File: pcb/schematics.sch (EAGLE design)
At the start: 8 parts, among them IC1 MEGA8-P

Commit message: Update pcb
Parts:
- removed MICROUSB: 1X5, adafruit:1X5
- removed RTC: 1X4-3.5MM, adafruit:1X4-3.5MM
- removed S1: (no value), switch-omron:40-XX
- added BTN: (no value), switch-omron:10-XX
- added X1, X2: 22-23-2051, con-molex:22-23-2051
- SOIL: value 1X4-3.5MM -> 1X4-BIG; device adafruit:1X4-3.5MM -> adafruit:1X4-BIG
- renumbered R1 to BTNR
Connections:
- new net N$9: IC1.PC0(ADC0), SOIL.4
- net N$1: now also X1-4.S; no longer RTC.3
- net N$2: now also X1-3.S; no longer RTC.2
- net N$3: now also IC1.GND, X1-1.S, X2-1.S; no longer MICROUSB.1, RTC.1
- net N$5: now also BTN.S1, IC1.AVCC, X1-5.S, X2-5.S; no longer MICROUSB.5, RTC.4, S1.S1, SOIL.1
- net N$6: now also SOIL.1; no longer SOIL.4
- net N$7: now also BTN.S; no longer S1.S
- net N$8: now also BTN.P; no longer S1.P
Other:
- moved on the sheet: SOIL

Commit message: Update eagle files
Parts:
- added C1: (no value), rcl:C-EU025-025X050
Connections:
- removed net N$3: BTNR.2, IC1.GND, IC1.GND@1, SOIL.2, U$1.GND, U$2.GND, X1-1.S, X2-1.S
- new net GND: BTNR.2, C1.2, IC1.GND, IC1.GND@1, SOIL.2, U$1.GND, U$2.GND, X1-1.S, X2-1.S
- net N$5: now also C1.1
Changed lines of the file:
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@@
 <part name="X1" library="con-molex" library_urn="urn:adsk.eagle:library:165" deviceset="22-23-2051" device="" package3d_urn="urn:adsk.eagle:package:8078636/1"/>
 <part name="X2" library="con-molex" library_urn="urn:adsk.eagle:library:165" deviceset="22-23-2051" device="" package3d_urn="urn:adsk.eagle:package:8078636/1"/>
+<part name="C1" library="rcl" library_urn="urn:adsk.eagle:library:334" deviceset="C-EU" device="025-025X050" package3d_urn="urn:adsk.eagle:package:23629/2"/>
 </parts>
 <sheets>
@@
 <instance part="X2" gate="-5" x="-101.6" y="83.82" smashed="yes" rot="R180">
 <attribute name="NAME" x="-104.14" y="84.582" size="1.524" layer="95" rot="R180"/>
+</instance>
+<instance part="C1" gate="G$1" x="-91.44" y="78.74" smashed="yes">
+<attribute name="NAME" x="-89.916" y="79.121" size="1.778" layer="95"/>
+<attribute name="VALUE" x="-89.916" y="74.041" size="1.778" layer="96"/>
 </instance>
 </instances>
@@
 </segment>
 </net>
-<net name="N$3" class="0">
+<net name="GND" class="0">
 <segment>
 <pinref part="U$2" gate="G$1" pin="GND"/>
@@
 <wire x1="38.1" y1="33.02" x2="25.4" y2="33.02" width="0.1524" layer="91"/>
 <wire x1="25.4" y1="33.02" x2="25.4" y2="48.26" width="0.1524" layer="91"/>
-<wire x1="-99.06" y1="73.66" x2="-71.12" y2="73.66" width="0.1524" layer="91"/>
+<wire x1="-99.06" y1="73.66" x2="-91.44" y2="73.66" width="0.1524" layer="91"/>
 <junction x="-71.12" y="73.66"/>
 <pinref part="IC1" gate="G$1" pin="GND"/>
+<wire x1="-91.44" y1="73.66" x2="-71.12" y2="73.66" width="0.1524" layer="91"/>
 <wire x1="-71.12" y1="83.82" x2="-71.12" y2="109.22" width="0.1524" layer="91"/>
 <wire x1="-71.12" y1="109.22" x2="-63.5" y2="109.22" width="0.1524" layer="91"/>
@@
 <wire x1="38.1" y1="35.56" x2="43.18" y2="35.56" width="0.1524" layer="91"/>
 <pinref part="X2" gate="-1" pin="S"/>
+<pinref part="C1" gate="G$1" pin="2"/>
+<junction x="-91.44" y="73.66"/>
+<label x="-99.06" y="73.66" size="1.778" layer="95"/>
 </segment>
 </net>
@@
 <pinref part="X1" gate="-5" pin="S"/>
 <pinref part="X2" gate="-5" pin="S"/>
-<wire x1="-83.82" y1="83.82" x2="-99.06" y2="83.82" width="0.1524" layer="91"/>
+<wire x1="-83.82" y1="83.82" x2="-91.44" y2="83.82" width="0.1524" layer="91"/>
+<pinref part="C1" gate="G$1" pin="1"/>
+<wire x1="-91.44" y1="83.82" x2="-99.06" y2="83.82" width="0.1524" layer="91"/>
+<wire x1="-91.44" y1="81.28" x2="-91.44" y2="83.82" width="0.1524" layer="91"/>
+<junction x="-91.44" y="83.82"/>
 </segment>
 </net>
@@
 packages will not be understood (or retained) with this version.
 </note>
+<note version="8.4" severity="warning">
+Since Version 8.4, EAGLE supports properties for SPICE simulation.
+Probes in schematics and SPICE mapping objects found in parts and library devices
+will not be understood with this version. Update EAGLE to the latest version
+for full support of SPICE simulation.
+</note>
 </compatibility>

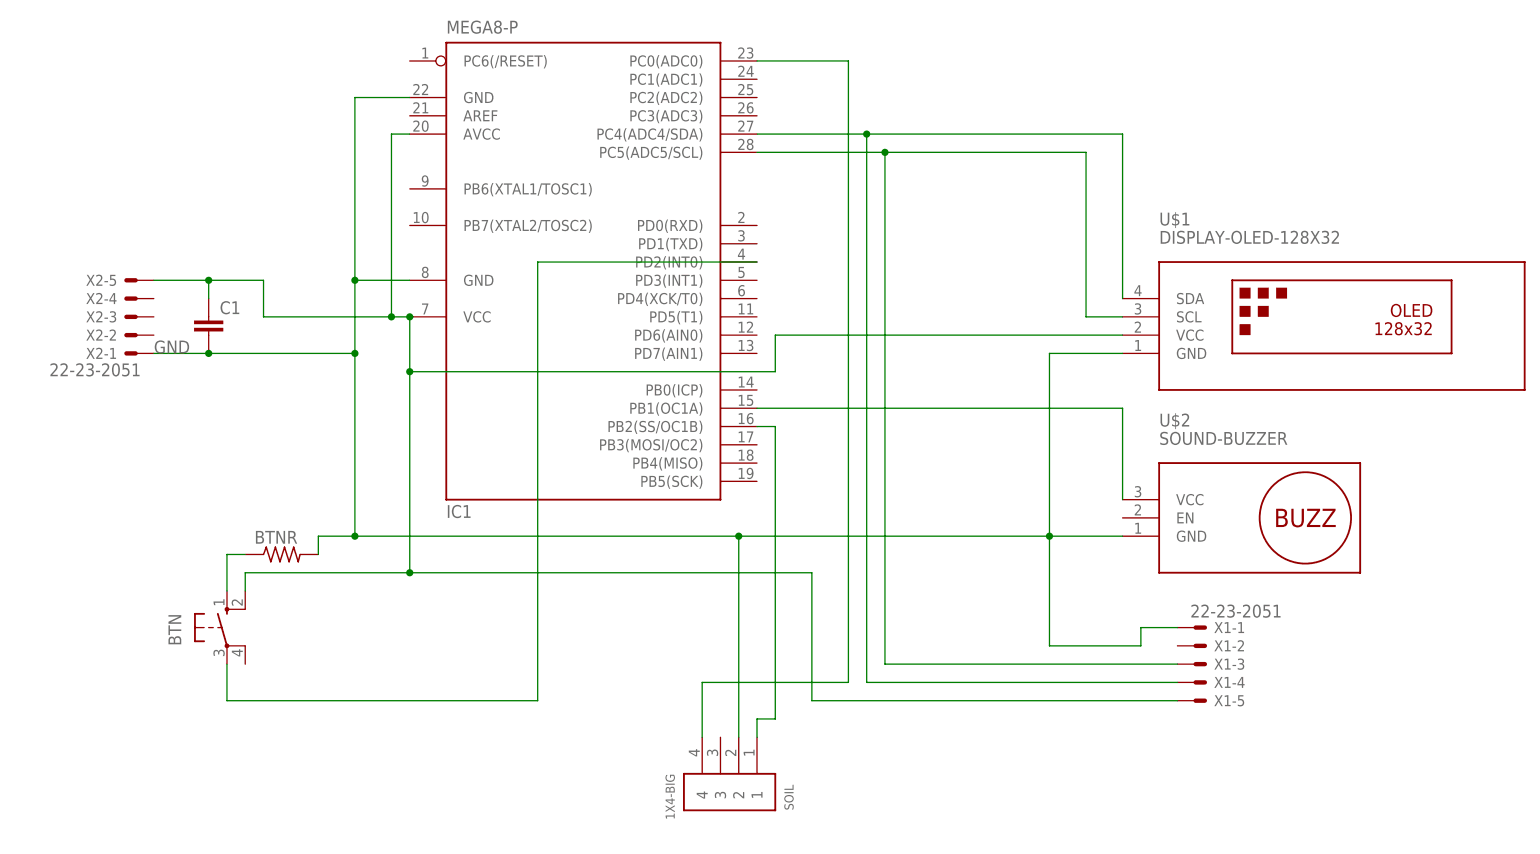
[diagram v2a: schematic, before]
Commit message: Add slide switch
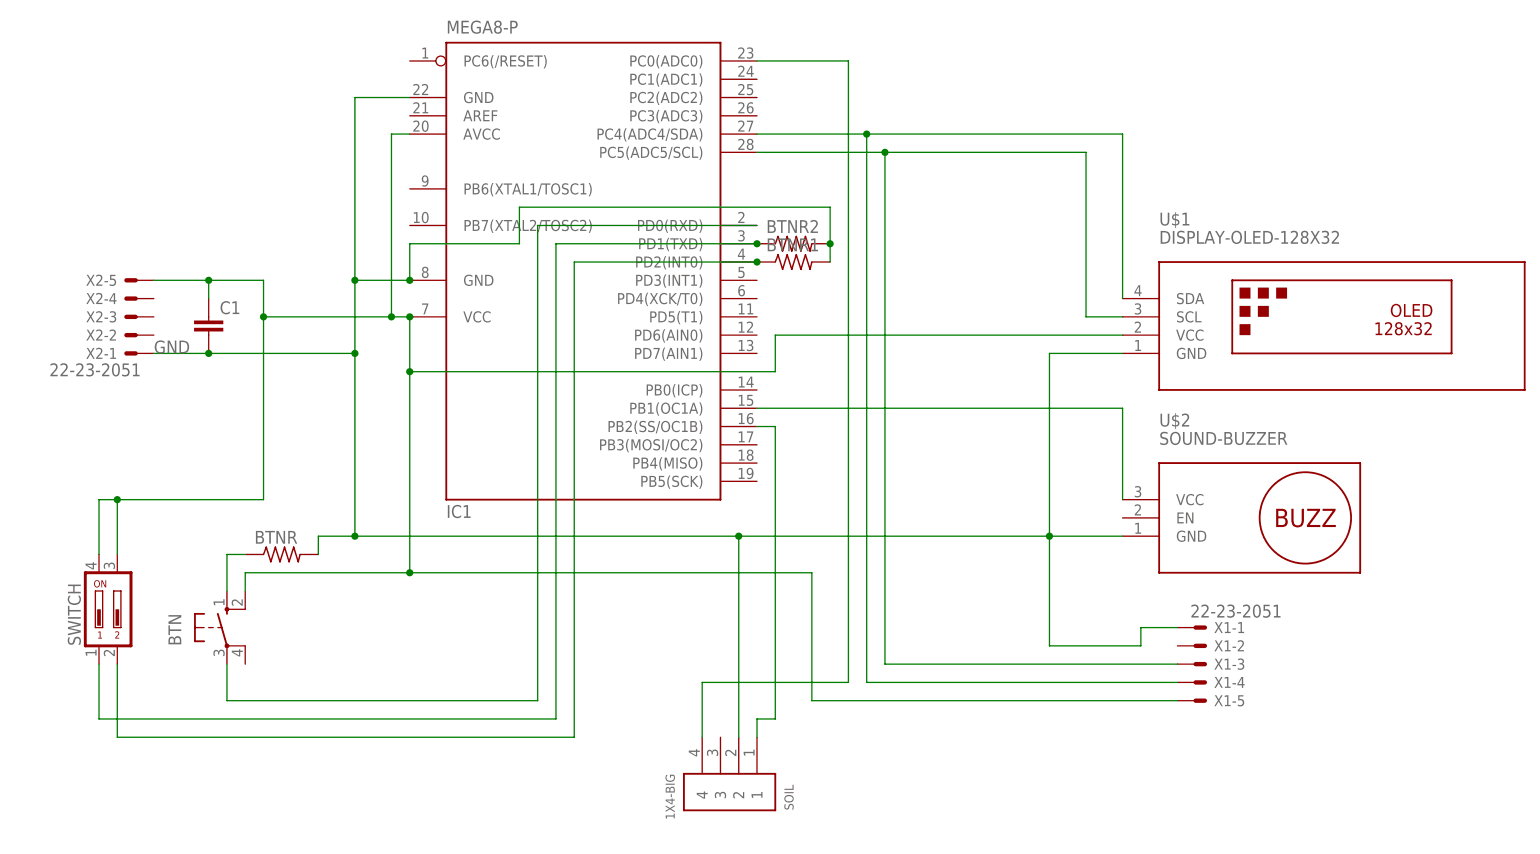
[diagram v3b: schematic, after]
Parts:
- added BTNR1, BTNR2: (no value), adafruit:R-US_0204/7
- added SWITCH: (no value), switch-dil:DIP02YL
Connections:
- new net N$10: BTNR1.1, IC1.PD2(INT0), SWITCH.2
- new net N$3: BTNR2.1, IC1.PD1(TXD), SWITCH.1
- net GND: now also BTNR1.2, BTNR2.2
- net N$5: now also SWITCH.3, SWITCH.4
- net N$8: now also IC1.PD0(RXD); no longer IC1.PD2(INT0)
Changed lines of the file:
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@@
 <part name="X2" library="con-molex" library_urn="urn:adsk.eagle:library:165" deviceset="22-23-2051" device="" package3d_urn="urn:adsk.eagle:package:8078636/1"/>
 <part name="C1" library="rcl" library_urn="urn:adsk.eagle:library:334" deviceset="C-EU" device="025-025X050" package3d_urn="urn:adsk.eagle:package:23629/2"/>
+<part name="SWITCH" library="switch-dil" library_urn="urn:adsk.eagle:library:375" deviceset="DIP02YL" device="" package3d_urn="urn:adsk.eagle:package:27254/2"/>
+<part name="BTNR1" library="adafruit" library_urn="urn:adsk.eagle:library:420" deviceset="R-US_" device="0204/7" package3d_urn="urn:adsk.eagle:package:6240596/1"/>
+<part name="BTNR2" library="adafruit" library_urn="urn:adsk.eagle:library:420" deviceset="R-US_" device="0204/7" package3d_urn="urn:adsk.eagle:package:6240596/1"/>
 </parts>
 <sheets>
@@
 <attribute name="NAME" x="-89.916" y="79.121" size="1.778" layer="95"/>
 <attribute name="VALUE" x="-89.916" y="74.041" size="1.778" layer="96"/>
+</instance>
+<instance part="SWITCH" gate="1" x="-106.68" y="38.1" smashed="yes">
+<attribute name="NAME" x="-109.22" y="33.02" size="1.778" layer="95" rot="R90"/>
+<attribute name="VALUE" x="-99.695" y="33.02" size="1.778" layer="96" rot="R90"/>
+</instance>
+<instance part="BTNR1" gate="G$1" x="-10.16" y="86.36" smashed="yes">
+<attribute name="NAME" x="-13.97" y="87.8586" size="1.778" layer="95"/>
+<attribute name="VALUE" x="-13.97" y="83.058" size="1.778" layer="96"/>
+</instance>
+<instance part="BTNR2" gate="G$1" x="-10.16" y="88.9" smashed="yes">
+<attribute name="NAME" x="-13.97" y="90.3986" size="1.778" layer="95"/>
+<attribute name="VALUE" x="-13.97" y="85.598" size="1.778" layer="96"/>
 </instance>
 </instances>
@@
 <junction x="-91.44" y="73.66"/>
 <label x="-99.06" y="73.66" size="1.778" layer="95"/>
+<wire x1="-63.5" y1="83.82" x2="-63.5" y2="88.9" width="0.1524" layer="91"/>
+<wire x1="-63.5" y1="88.9" x2="-48.26" y2="88.9" width="0.1524" layer="91"/>
+<junction x="-63.5" y="83.82"/>
+<wire x1="-48.26" y1="88.9" x2="-48.26" y2="93.98" width="0.1524" layer="91"/>
+<wire x1="-48.26" y1="93.98" x2="-5.08" y2="93.98" width="0.1524" layer="91"/>
+<pinref part="BTNR2" gate="G$1" pin="2"/>
+<wire x1="-5.08" y1="93.98" x2="-5.08" y2="88.9" width="0.1524" layer="91"/>
+<pinref part="BTNR1" gate="G$1" pin="2"/>
+<wire x1="-5.08" y1="86.36" x2="-5.08" y2="88.9" width="0.1524" layer="91"/>
+<junction x="-5.08" y="88.9"/>
 </segment>
 </net>
@@
 <wire x1="-91.44" y1="81.28" x2="-91.44" y2="83.82" width="0.1524" layer="91"/>
 <junction x="-91.44" y="83.82"/>
+<wire x1="-83.82" y1="78.74" x2="-83.82" y2="53.34" width="0.1524" layer="91"/>
+<junction x="-83.82" y="78.74"/>
+<pinref part="SWITCH" gate="1" pin="4"/>
+<wire x1="-83.82" y1="53.34" x2="-104.14" y2="53.34" width="0.1524" layer="91"/>
+<wire x1="-104.14" y1="53.34" x2="-106.68" y2="53.34" width="0.1524" layer="91"/>
+<wire x1="-106.68" y1="53.34" x2="-106.68" y2="45.72" width="0.1524" layer="91"/>
+<pinref part="SWITCH" gate="1" pin="3"/>
+<wire x1="-104.14" y1="45.72" x2="-104.14" y2="53.34" width="0.1524" layer="91"/>
+<junction x="-104.14" y="53.34"/>
 </segment>
 </net>
@@
 <net name="N$8" class="0">
 <segment>
-<pinref part="IC1" gate="G$1" pin="PD2(INT0)"/>
-<wire x1="-15.24" y1="86.36" x2="-45.72" y2="86.36" width="0.1524" layer="91"/>
-<wire x1="-45.72" y1="86.36" x2="-45.72" y2="25.4" width="0.1524" layer="91"/>
+<wire x1="-45.72" y1="91.44" x2="-45.72" y2="25.4" width="0.1524" layer="91"/>
 <wire x1="-45.72" y1="25.4" x2="-88.9" y2="25.4" width="0.1524" layer="91"/>
 <pinref part="BTN" gate="1" pin="P"/>
 <wire x1="-88.9" y1="25.4" x2="-88.9" y2="30.48" width="0.1524" layer="91"/>
+<pinref part="IC1" gate="G$1" pin="PD0(RXD)"/>
+<wire x1="-45.72" y1="91.44" x2="-15.24" y2="91.44" width="0.1524" layer="91"/>
 </segment>
 </net>
@@
 </segment>
 </net>
+<net name="N$3" class="0">
+<segment>
+<pinref part="IC1" gate="G$1" pin="PD1(TXD)"/>
+<wire x1="-15.24" y1="88.9" x2="-43.18" y2="88.9" width="0.1524" layer="91"/>
+<wire x1="-43.18" y1="88.9" x2="-43.18" y2="22.86" width="0.1524" layer="91"/>
+<pinref part="SWITCH" gate="1" pin="1"/>
+<wire x1="-43.18" y1="22.86" x2="-106.68" y2="22.86" width="0.1524" layer="91"/>
+<wire x1="-106.68" y1="22.86" x2="-106.68" y2="30.48" width="0.1524" layer="91"/>
+<pinref part="BTNR2" gate="G$1" pin="1"/>
+<junction x="-15.24" y="88.9"/>
+</segment>
+</net>
+<net name="N$10" class="0">
+<segment>
+<pinref part="SWITCH" gate="1" pin="2"/>
+<wire x1="-104.14" y1="30.48" x2="-104.14" y2="20.32" width="0.1524" layer="91"/>
+<wire x1="-104.14" y1="20.32" x2="-40.64" y2="20.32" width="0.1524" layer="91"/>
+<pinref part="IC1" gate="G$1" pin="PD2(INT0)"/>
+<wire x1="-40.64" y1="20.32" x2="-40.64" y2="86.36" width="0.1524" layer="91"/>
+<wire x1="-40.64" y1="86.36" x2="-15.24" y2="86.36" width="0.1524" layer="91"/>
+<pinref part="BTNR1" gate="G$1" pin="1"/>
+<junction x="-15.24" y="86.36"/>
+</segment>
+</net>

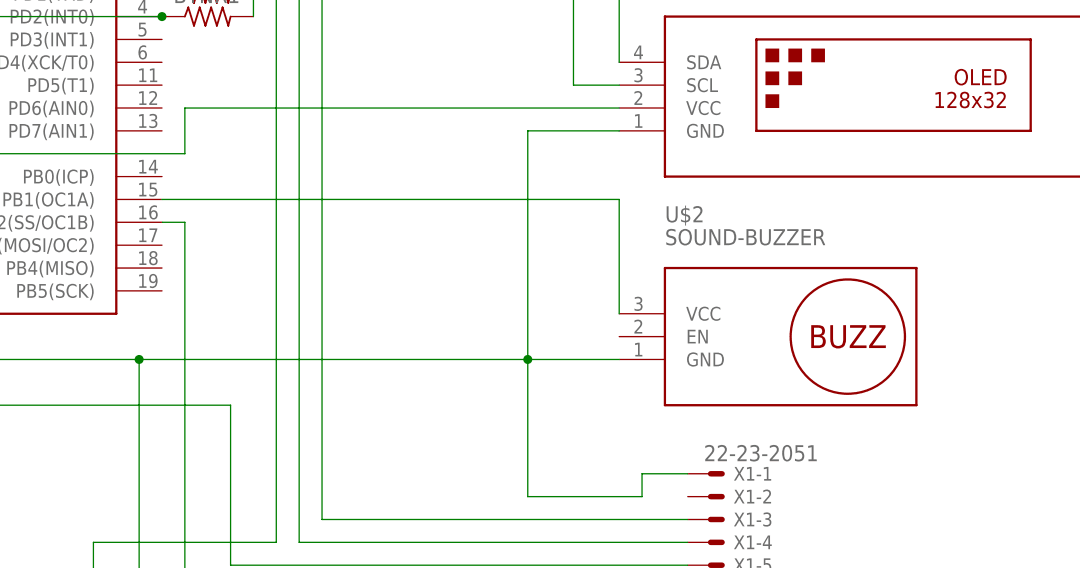
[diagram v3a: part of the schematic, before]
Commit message: Upadate pcb to use passive buzzer
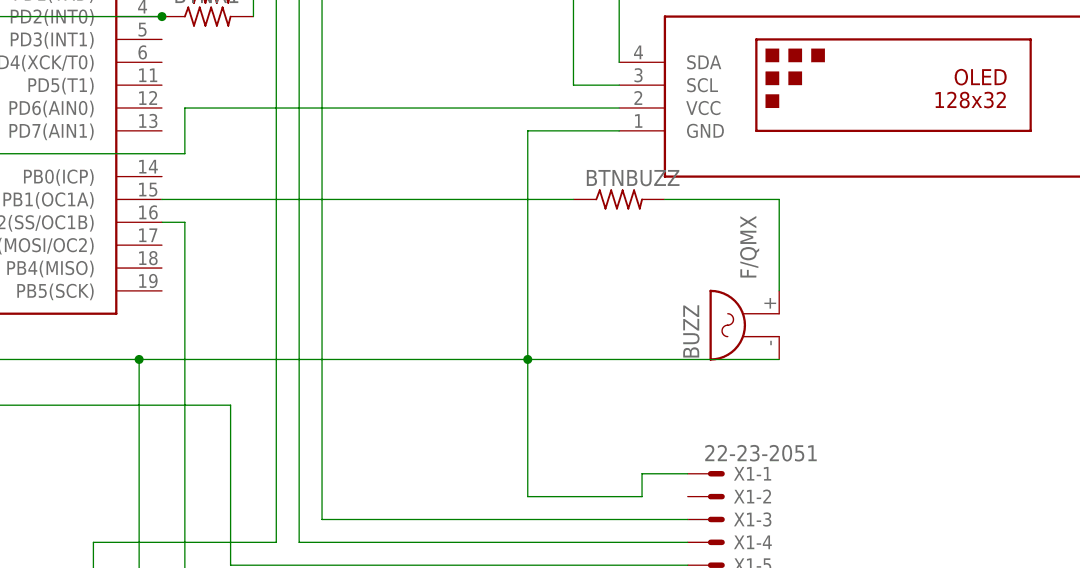
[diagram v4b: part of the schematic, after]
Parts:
- removed U$2: SOUND-BUZZER, diy-modules:SOUND-BUZZER
- added BTNBUZZ: (no value), adafruit:R-US_0204/7
- added BUZZ: F/QMX, buzzer:F/QMX
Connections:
- new net N$11: BTNBUZZ.2, BUZZ.2
- net GND: now also BUZZ.1; no longer U$2.GND
- net N$4: now also BTNBUZZ.1; no longer U$2.VCC
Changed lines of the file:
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@@
 <part name="U$1" library="diy-modules" deviceset="DISPLAY-OLED-128X32" device=""/>
 <part name="IC1" library="atmel" library_urn="urn:adsk.eagle:library:105" deviceset="MEGA8-P" device="" package3d_urn="urn:adsk.eagle:package:4320/1"/>
-<part name="U$2" library="diy-modules" deviceset="SOUND-BUZZER" device=""/>
 <part name="BTNR" library="adafruit" library_urn="urn:adsk.eagle:library:420" deviceset="R-US_" device="0204/7" package3d_urn="urn:adsk.eagle:package:6240596/1"/>
 <part name="BTN" library="switch-omron" library_urn="urn:adsk.eagle:library:377" deviceset="10-XX" device="" package3d_urn="urn:adsk.eagle:package:27496/1"/>
@@
 <part name="BTNR1" library="adafruit" library_urn="urn:adsk.eagle:library:420" deviceset="R-US_" device="0204/7" package3d_urn="urn:adsk.eagle:package:6240596/1"/>
 <part name="BTNR2" library="adafruit" library_urn="urn:adsk.eagle:library:420" deviceset="R-US_" device="0204/7" package3d_urn="urn:adsk.eagle:package:6240596/1"/>
+<part name="BUZZ" library="buzzer" library_urn="urn:adsk.eagle:library:113" deviceset="F/QMX" device="" package3d_urn="urn:adsk.eagle:package:5278/1"/>
+<part name="BTNBUZZ" library="adafruit" library_urn="urn:adsk.eagle:library:420" deviceset="R-US_" device="0204/7" package3d_urn="urn:adsk.eagle:package:6240596/1"/>
 </parts>
 <sheets>
@@
 <attribute name="VALUE" x="-58.42" y="118.11" size="1.778" layer="96"/>
 </instance>
-<instance part="U$2" gate="G$1" x="53.34" y="50.8" smashed="yes">
-<attribute name="NAME" x="40.64" y="63.5" size="1.778" layer="95"/>
-<attribute name="VALUE" x="40.64" y="60.96" size="1.778" layer="96"/>
-</instance>
 <instance part="BTNR" gate="G$1" x="-81.28" y="45.72" smashed="yes">
 <attribute name="NAME" x="-85.09" y="47.2186" size="1.778" layer="95"/>
@@
 <attribute name="NAME" x="-13.97" y="90.3986" size="1.778" layer="95"/>
 <attribute name="VALUE" x="-13.97" y="85.598" size="1.778" layer="96"/>
+</instance>
+<instance part="BUZZ" gate="G$1" x="50.8" y="50.8" smashed="yes" rot="R90">
+<attribute name="NAME" x="44.45" y="48.26" size="1.778" layer="95" rot="R90"/>
+<attribute name="VALUE" x="50.8" y="57.15" size="1.778" layer="96" rot="R90"/>
+</instance>
+<instance part="BTNBUZZ" gate="G$1" x="35.56" y="66.04" smashed="yes">
+<attribute name="NAME" x="31.75" y="67.5386" size="1.778" layer="95"/>
+<attribute name="VALUE" x="31.75" y="62.738" size="1.778" layer="96"/>
 </instance>
 </instances>
@@
 <net name="GND" class="0">
 <segment>
-<pinref part="U$2" gate="G$1" pin="GND"/>
-<wire x1="35.56" y1="48.26" x2="25.4" y2="48.26" width="0.1524" layer="91"/>
 <pinref part="IC1" gate="G$1" pin="GND@1"/>
 <wire x1="25.4" y1="48.26" x2="-17.78" y2="48.26" width="0.1524" layer="91"/>
@@
 <wire x1="-5.08" y1="86.36" x2="-5.08" y2="88.9" width="0.1524" layer="91"/>
 <junction x="-5.08" y="88.9"/>
+<pinref part="BUZZ" gate="G$1" pin="1"/>
+<wire x1="25.4" y1="48.26" x2="53.34" y2="48.26" width="0.1524" layer="91"/>
 </segment>
 </net>
@@
 <segment>
 <pinref part="IC1" gate="G$1" pin="PB1(OC1A)"/>
-<pinref part="U$2" gate="G$1" pin="VCC"/>
-<wire x1="-15.24" y1="66.04" x2="35.56" y2="66.04" width="0.1524" layer="91"/>
-<wire x1="35.56" y1="66.04" x2="35.56" y2="53.34" width="0.1524" layer="91"/>
+<wire x1="-15.24" y1="66.04" x2="30.48" y2="66.04" width="0.1524" layer="91"/>
+<pinref part="BTNBUZZ" gate="G$1" pin="1"/>
 </segment>
 </net>
@@
 </segment>
 </net>
+<net name="N$11" class="0">
+<segment>
+<pinref part="BUZZ" gate="G$1" pin="2"/>
+<pinref part="BTNBUZZ" gate="G$1" pin="2"/>
+<wire x1="53.34" y1="55.88" x2="53.34" y2="66.04" width="0.1524" layer="91"/>
+<wire x1="53.34" y1="66.04" x2="40.64" y2="66.04" width="0.1524" layer="91"/>
+</segment>
+</net>
